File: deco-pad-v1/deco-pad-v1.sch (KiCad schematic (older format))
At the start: 70 parts, among them J1 AVR-ISP-6, SW1 EC11, SW2 SW_Push, U1 PRTR5VOU2X, U2 ATmega32U4-MU, Y1 16MHz

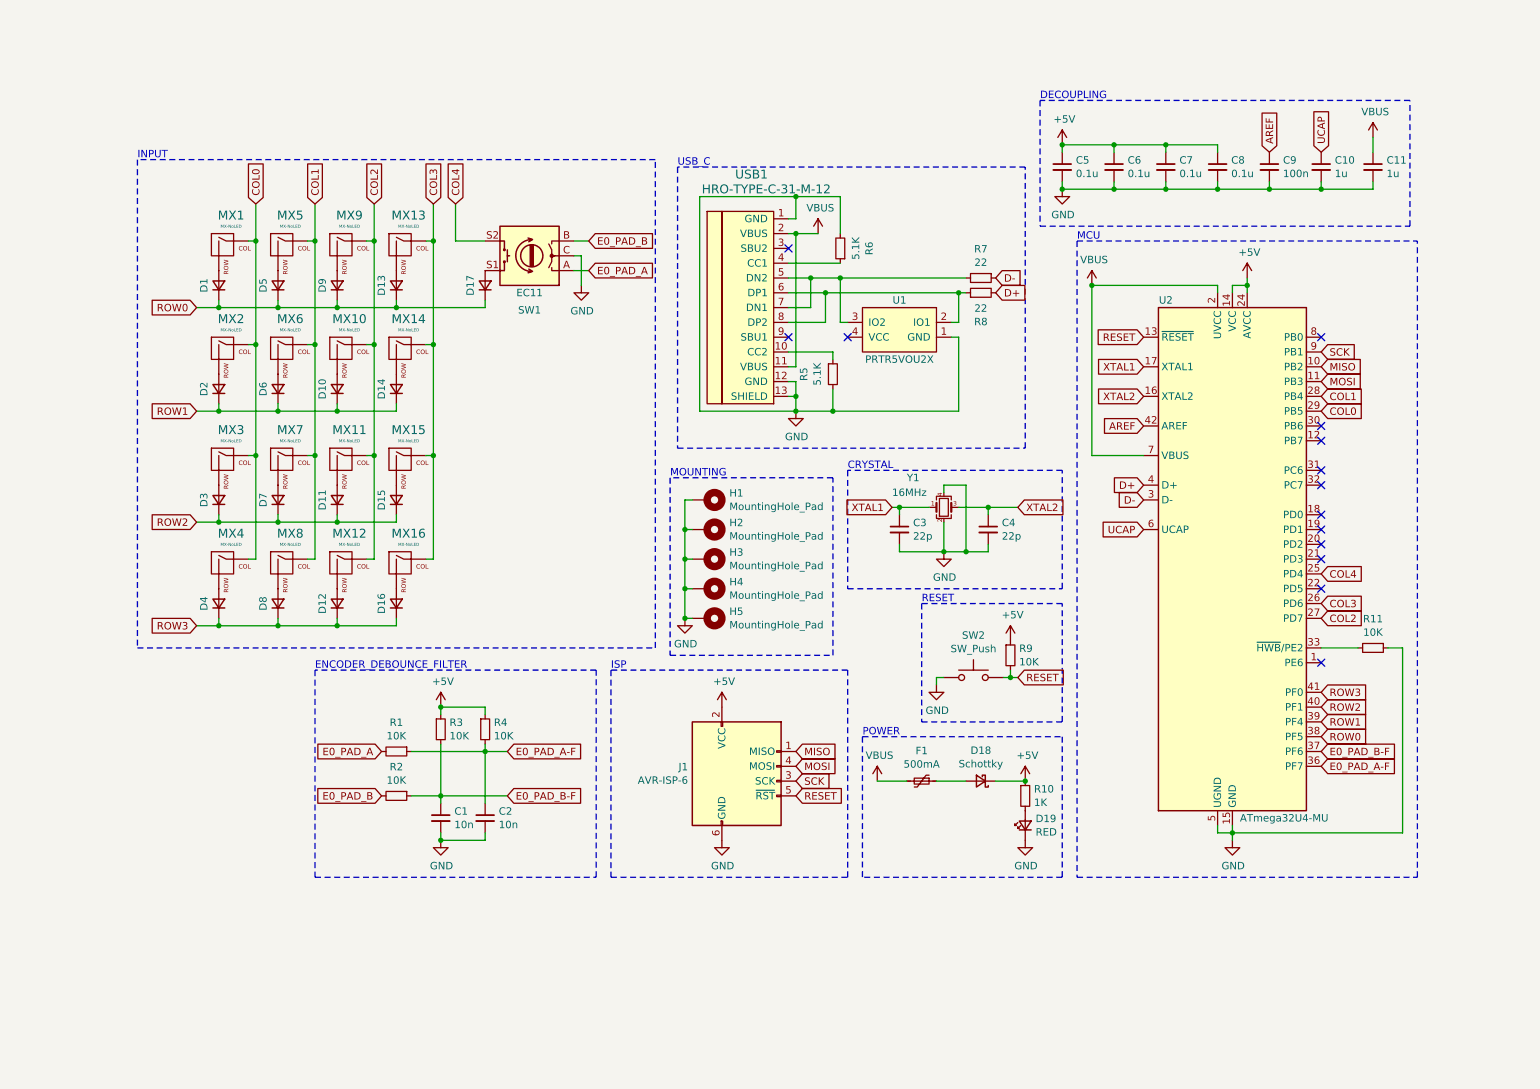
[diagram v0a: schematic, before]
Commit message: [NZ] Removed ESD while research a backup. Remove schottky since not needed and would drop the voltage too much. Some cleanup. Will add silk art and curved tracks next.
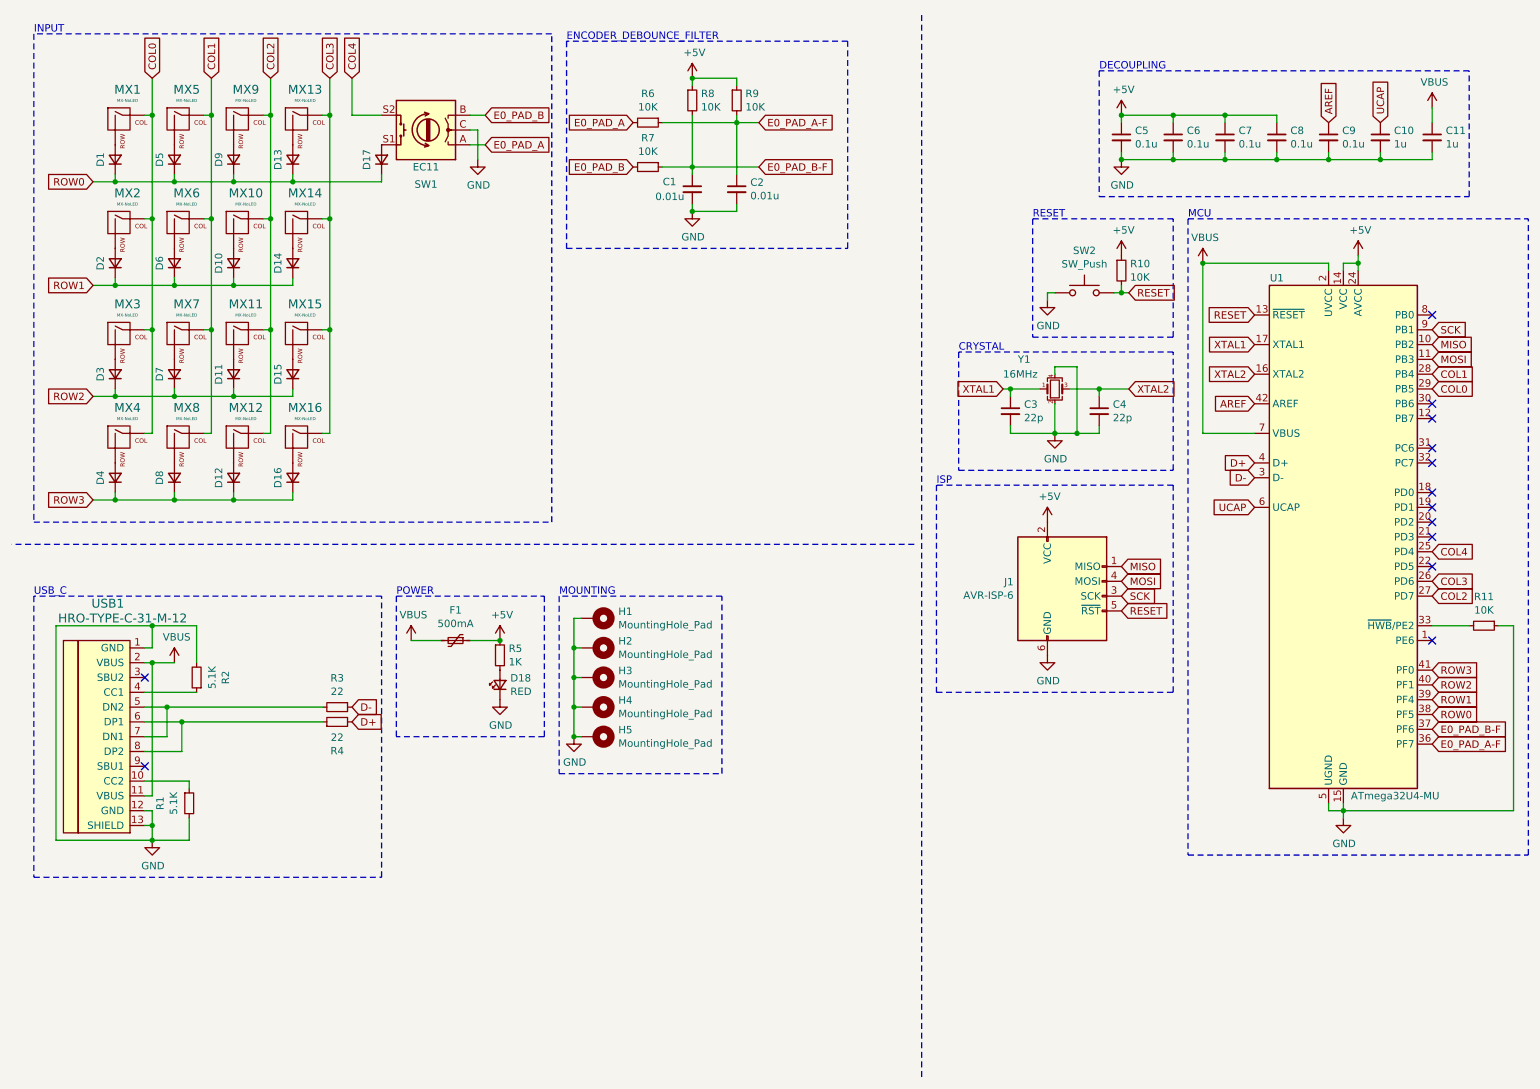
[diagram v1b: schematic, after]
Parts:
- removed D18: Schottky, Diode_SMD:D_SOD-123, symbol Device:D_Schottky_Small
- removed U1: PRTR5VOU2X, Nexperia:SOT143B, symbol prtr5vou2x:PRTR5VOU2X
- C1, C2: value 10n -> 0.01u
- C9: value 100n -> 0.1u
- renumbered D19 to D18, R5 to R1, R9 to R10, R6 to R2, R7 to R3, R8 to R4, R10 to R5, R1 to R6, R2 to R7, R3 to R8, R4 to R9, U2 to U1
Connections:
- net +5V: now also F1.1
- no-connect marks 14 -> 13
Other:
- moved on the sheet: C1, C10, C11, C2, C3, C4, C5, C6, C7, C8, C9, D1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
